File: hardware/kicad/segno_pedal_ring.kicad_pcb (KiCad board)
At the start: 2 copper layers, 80 x 80 mm, 17 parts, among them J1 Conn_01x04, J2 NEOPIXEL, J3 RINGPINS24, U1 XIAO-RP2350, U2 74AHCT125N

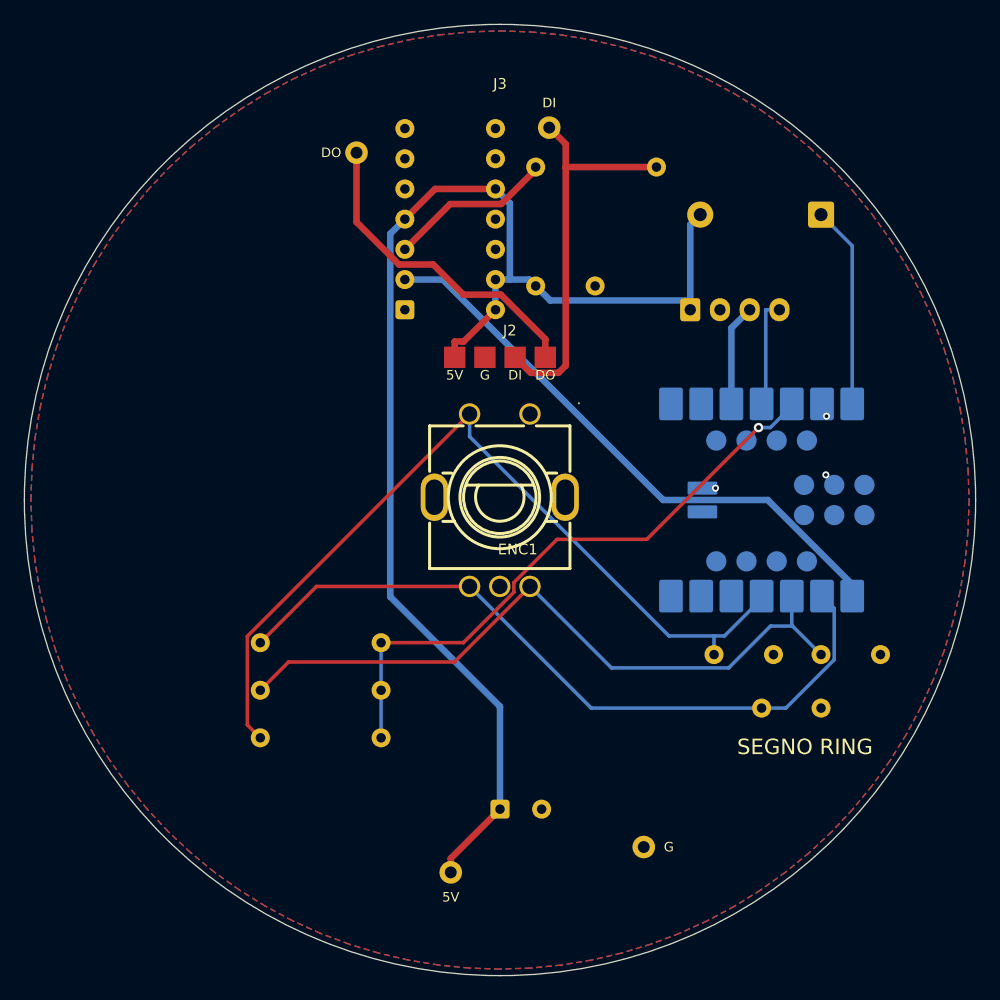
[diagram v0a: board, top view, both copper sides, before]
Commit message: feat(hardware): keep the Ring 16 pad circle too, and model the mount pins
Two owner calls.

**J4 -- the Ring 16 bolt circle stays on the board.** Same four signals in the
same JP order (the Ring 16's descr reads In/+5V/GND/Out = JP1/JP3/JP4/JP2, which
is J3's order), just r=21.05 against the Ring 24's r=31.59. Both pad sets sit on
the same nets and both get routed, so either ring is connected as-fabbed and
swapping one for the other needs no respin. That is not a short: exactly one ring
is ever fitted. They can coexist because the Ring 16's r=21.05 circle falls
INSIDE a Ring 24's O52.3 bore -- fit the 24 and the 16's pads simply sit exposed
in the bore.

J4's pads are fixed geometry, so the movable parts yielded to them: pad 2 landed
2.08 mm inside R2, and pad 4 came within 0.2 mm of C5. R2/R3/R4 moved x 26 -> 32
and C5 y 18 -> 18.5. Every decoupling anchor still holds (C5->U2.14 3.70,
C3->U1.3 5.50, C4->U1.4 6.34 mm).

**The mount pins are modelled.** Four PinHeader_1x01 models on RING1, one per J3
pad, so the render shows what actually holds the module up instead of a ring
floating on nothing. KiCad's own header model confirms the standoff figure
independently: its plastic insulator spans exactly z 0..2.54, which is the 2.54
already applied to the ring's own Z offset. Offsets are J3's pad positions with Y
NEGATED, because KiCad's 3D offset Y runs opposite to board Y.

The pins hang off RING1 rather than J3 because J3 carries
exclude_from_pos_files, and kicad-cli's renderer silently skips the models of any
footprint with that flag (the trap from the previous commit).

Note the drill file CHANGED: J4 adds four 1.9 mm plated holes. Gerbers
regenerated.

Verified: DRC 0 errors, 0 unconnected after a full re-route (optimiser +50.7%);
0 pad-net mismatches; no courtyard clashes; nothing off the O80 disc; both
--selftest suites green.

Refs #987
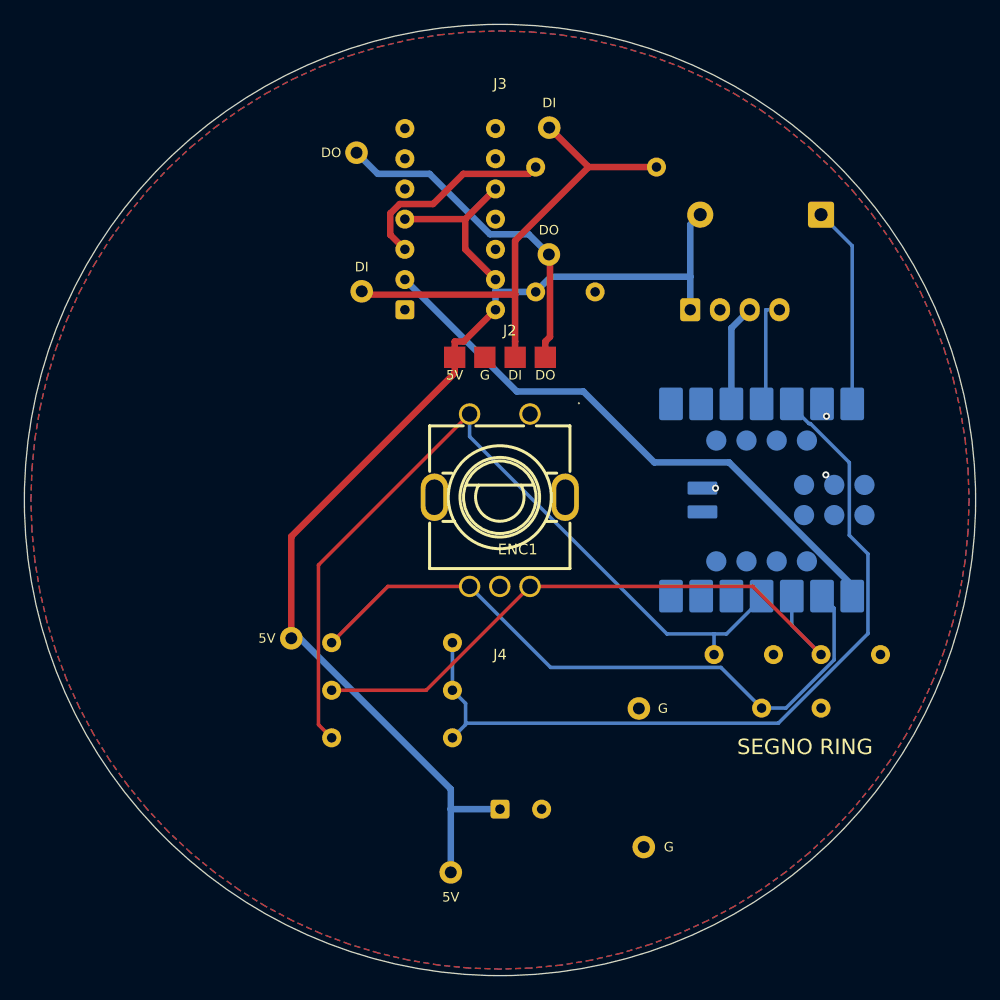
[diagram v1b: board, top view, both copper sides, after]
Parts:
- added J4: RINGPINS16, ModuleMountPads_4, F.Cu at (36.0, 36.0)
- moved R2 6.00 mm to (32.0, 48.0)
- moved R3 6.00 mm to (32.0, 52.0)
- moved R4 6.00 mm to (32.0, 56.0)
- moved C5 0.50 mm to (39.0, 18.5)
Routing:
- net +3V3: track 51.4 -> 67.9 mm, vias 1 -> 0
- net RING_DATA: track 33.3 -> 42.0 mm
- net ENC_A: track 61.9 -> 55.9 mm
- net ENC_B: track 58.6 -> 53.1 mm
- net +5V_LED: track 111.6 -> 107.6 mm
- net RING_DATA_5V: track 14.0 -> 17.4 mm
- net ENC_SW: track 71.9 -> 69.5 mm
- net RING_DOUT: track 27.3 -> 28.6 mm

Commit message: fix(hardware): drop the XIAO's underside pads, trim the pins, carry both rings
Three owner calls.

**The XIAO's 16 UNDERSIDE pads are deleted** (15-30: D11..D18, SWDIO, SWDCLK,
EN, BOOT, a second 3V3_OUT, VBAT and two more GNDs). This board reflows the
module by its castellated edges only; nothing under the body is ever soldered,
and unsolderable copper directly beneath a module invites bridges and
intermittent contact rather than helping. The footprint is therefore NO LONGER
byte-verbatim from Seeed -- it is their geometry for pads 1-14 with 15-30
removed and nothing else touched, and the descr says so.

Knock-on: GND reached the module through pads 26/30 as well as 13. Those are
gone, so it is pad 13 alone -- which is the only GND on the side rows anyway --
and pad 13 keeps its own stitching via. Losing the underside GNDs also
disconnected the two pours from each other; DRC caught it, and eleven GND
stitching vias plus targeted vias into two isolated pockets close it. U1's part
symbol drops Conn_01x30 -> Conn_01x14 and XIAO_PADS now gates 1..14.

**The mount pins are trimmed.** KiCad's PinHeader_1x01 runs z -3.11..8.65 and
left 4.54 mm of bare pin standing above the ring, which nobody assembles -- you
snip them. PinHeader_1x01_trimmed.wrl is ours: insulator EXACTLY 0..2.54 (that
is the standoff and must not change) and the pin ending 1.0 mm proud of the
ring's top face. Authored in mm, so scale 1/2.54, the same convention
NeoPixel_Ring16's existing .wrl already uses here.

**Both rings are carried, switchable.** RING1 holds the Ring 24 on J3's r=31.59
circle (shown) and the Ring 16 on J4's r=21.05 circle (hidden), each with its
own four pins. Untick one group in the 3D viewer's model list and the board
shows the other build. Ring 16 is Adafruit's own STEP from the same MIT library,
measured O44.450 / O31.750 -- and J4's r=21.05 falls inside its r 15.9..22.2
material band, so the pads land under it correctly.

Note for anyone editing models from Python: pcbnew's Mo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
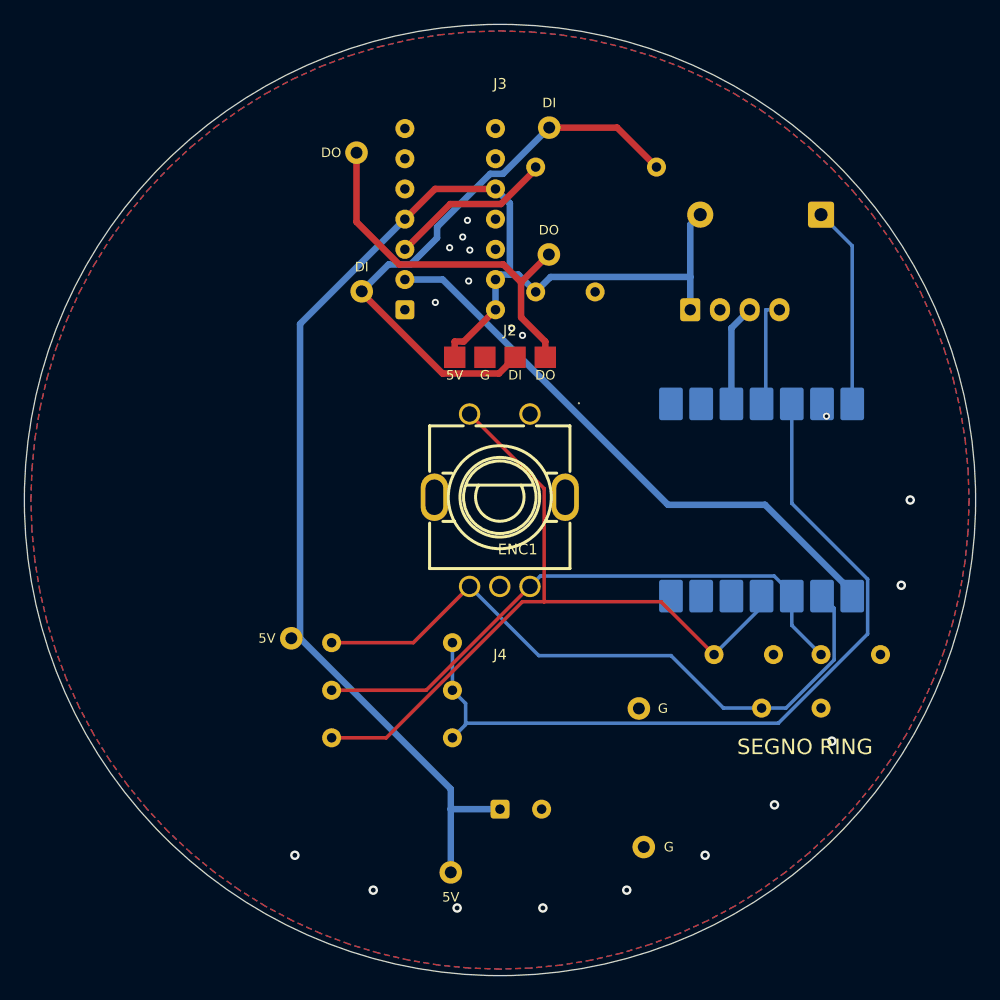
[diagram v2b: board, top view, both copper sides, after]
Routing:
- net +5V_LED: track 107.6 -> 119.5 mm
- net RING_DATA: track 42.0 -> 48.8 mm
- net ENC_SW: track 69.5 -> 63.7 mm
- net ENC_B: track 53.1 -> 49.4 mm
- net RING_DOUT: track 28.6 -> 32.2 mm
- net RING_DATA_5V: track 17.4 -> 14.0 mm
- net GND: vias 3 -> 19

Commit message: fix(hardware): the ring board routes clean, and keeps its ground stitching
The ring board's gerbers were not fabricable. DRC on the committed board
reported 45 violations: 26 clearance errors, 20 of them genuinely under
0.19 mm against the board's 0.2 mm rule and the worst at 0.1362 mm.

Two causes, both in route_ring_board.sh:

Freerouting was given the board's own 0.2 mm rule and lands a hair under
whatever it is given -- the exact trap route_console_board.sh documents and
routes around by exporting the DSN at 0.3 mm. This script never got that
fix. It now exports at 0.3 mm and keeps the 0.2 mm check, and sets via
geometry to the board's 0.8/0.4 rather than letting Freerouting fall back
to KiCad's 0.6/0.3 default, which is JLCPCB's minimum drill.

The rip-up removed the 19 hand-placed vias that are the only thing joining
the two GND pours, and Freerouting never puts them back because it routes
nets, not zones. Every run therefore produced "Missing connection between
items: Zone [GND] on F.Cu / Zone [GND] on B.Cu". The rip-up now removes
track segments only and leaves the vias in place, so they go into the DSN
as existing wiring and the router works around them. Restoring them after
the route instead does not work: the router has already used the space,
and 18 clearance and hole-clearance errors come back.

Now: 0 errors, 0 unconnected. The 19 remaining warnings are silkscreen --
18 of U1's own outline over its castellated pads and one ENC1 reference
overlap -- which fabs clip, and which are a footprint fix, not a routing one.
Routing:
- net RING_DATA: track 48.8 -> 61.2 mm
- net RING_DATA_5V: track 14.0 -> 21.4 mm
- net RING_DOUT: track 32.2 -> 36.3 mm, vias 0 -> 1
- net ENC_SW: track 63.7 -> 64.5 mm
- net LINK_TO_CONSOLE: track 9.21 -> 8.54 mm
- net +3V3: track 67.8 -> 68.4 mm

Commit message: fix(hardware): the ring board's vias and silkscreen come off the fab floor
Two findings from auditing both boards against the fab checklist, both on
the ring board; the console board came back clean on every check.

Nine of the twenty stitching vias were still KiCad's 0.6/0.3 default. That
is JLCPCB's MINIMUM drill, and route_console_board.sh already calls out why
sitting there for no reason is how a batch gets scrapped for a plating
fault. The rip-up step now normalises any kept via to the board's 0.8/0.4
BEFORE the DSN export, so the router works around the size that ships. All
twenty are now 0.8/0.4, and the front ground pour went from three islands
to one as a side effect.

U1's silkscreen outline ran straight through its own castellated pads: the
two long body edges sit at y 27.11 and 44.89 while the pad rows span
26.54..29.29 and 42.71..45.46, so both edges and all four corner arcs
crossed copper -- 18 silk_over_copper warnings. Those six shapes are gone;
the side edges, the USB outline and the pin-1 marker still describe the
part. ENC1's reference sat on its own silk circle and is moved clear.

The ring board now reports 0 errors, 0 warnings and 0 unconnected, where
the committed board reported 45 violations. Also verified, since nothing
in the toolchain checked it: the ring board's copper matches ring_board.py
pad for pad -- 61 pads, no extras on either side, no net mismatches.
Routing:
- net RING_DOUT: track 36.3 -> 41.2 mm
- net RING_DATA: track 61.2 -> 57.4 mm

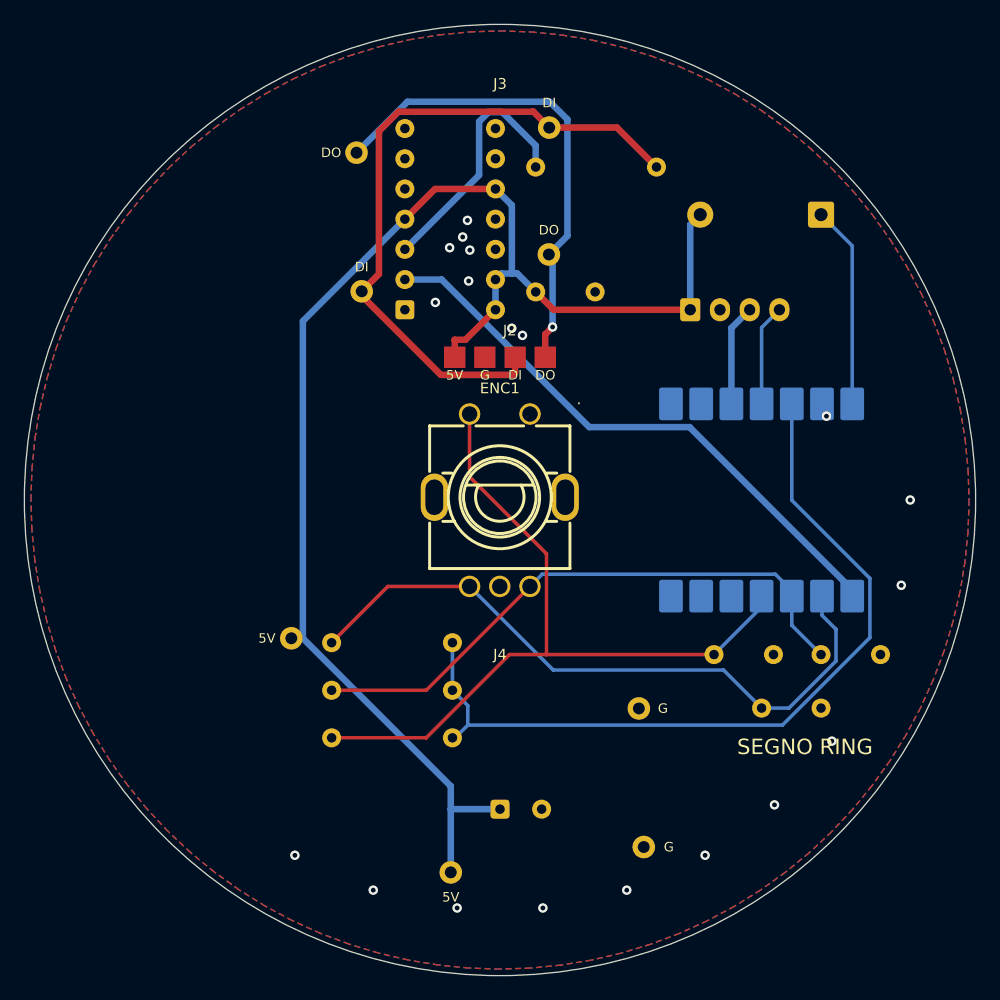
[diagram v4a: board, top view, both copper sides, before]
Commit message: feat(hardware): console board 5 V path for full-white LEDs, and pre-order review fixes (#1062)
Console board v3:
- J3 (5 V in) becomes a 2-pin JST VH; the pills move to one 3-pin JST VH J24
  (GND, DATA, +5V) whose +5V pad is bridged to J3's by a poured bar on both
  layers; J7 is retired. PILL_POWER gates the topology.
- VH 3D models generated by vh_models.py.
- Per-pin legends on the back silkscreen for J3 and J24, which read in
  opposite orders; PIN_LEGEND gates them.
- Committed gerbers and STEP brought up to date with the routed board.

Ring board:
- R5 100k holds the AHCT125 input low while the XIAO is not driving it, so
  the ring cannot latch random colours at power-up; RING_DATA_IDLE gates it.
- Rerouted, DRC clean, gerbers and STEP regenerated.
- The combined LCSC BOM describes the XIAO ring board instead of the old one.
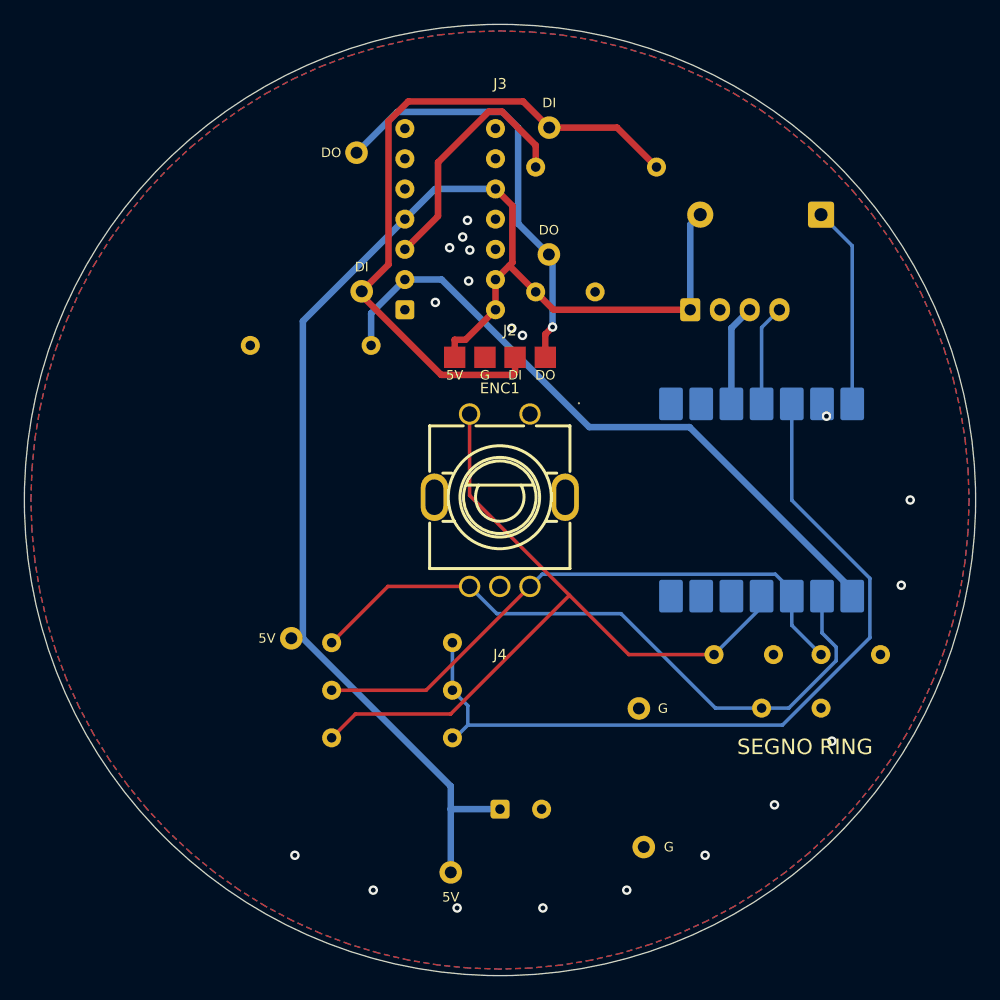
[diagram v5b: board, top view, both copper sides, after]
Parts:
- added R5: 100k, Resistor_THT:R_Axial_DIN0207_L6.3mm_D2.5mm_P10.16mm_Horizontal, B.Cu at (25.2, 23.0)
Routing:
- net RING_DATA_3V3: track 49.0 -> 55.7 mm
- net RING_DOUT: track 41.2 -> 36.3 mm
- net RING_DATA: track 57.4 -> 58.1 mm
